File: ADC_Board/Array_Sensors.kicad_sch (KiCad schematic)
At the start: 18 parts, among them U2 PAMC1350DWVR, U3 AMC1400QDWLRQ1, U4 AMC1400QDWLRQ1, U5 PAMC1350DWVR

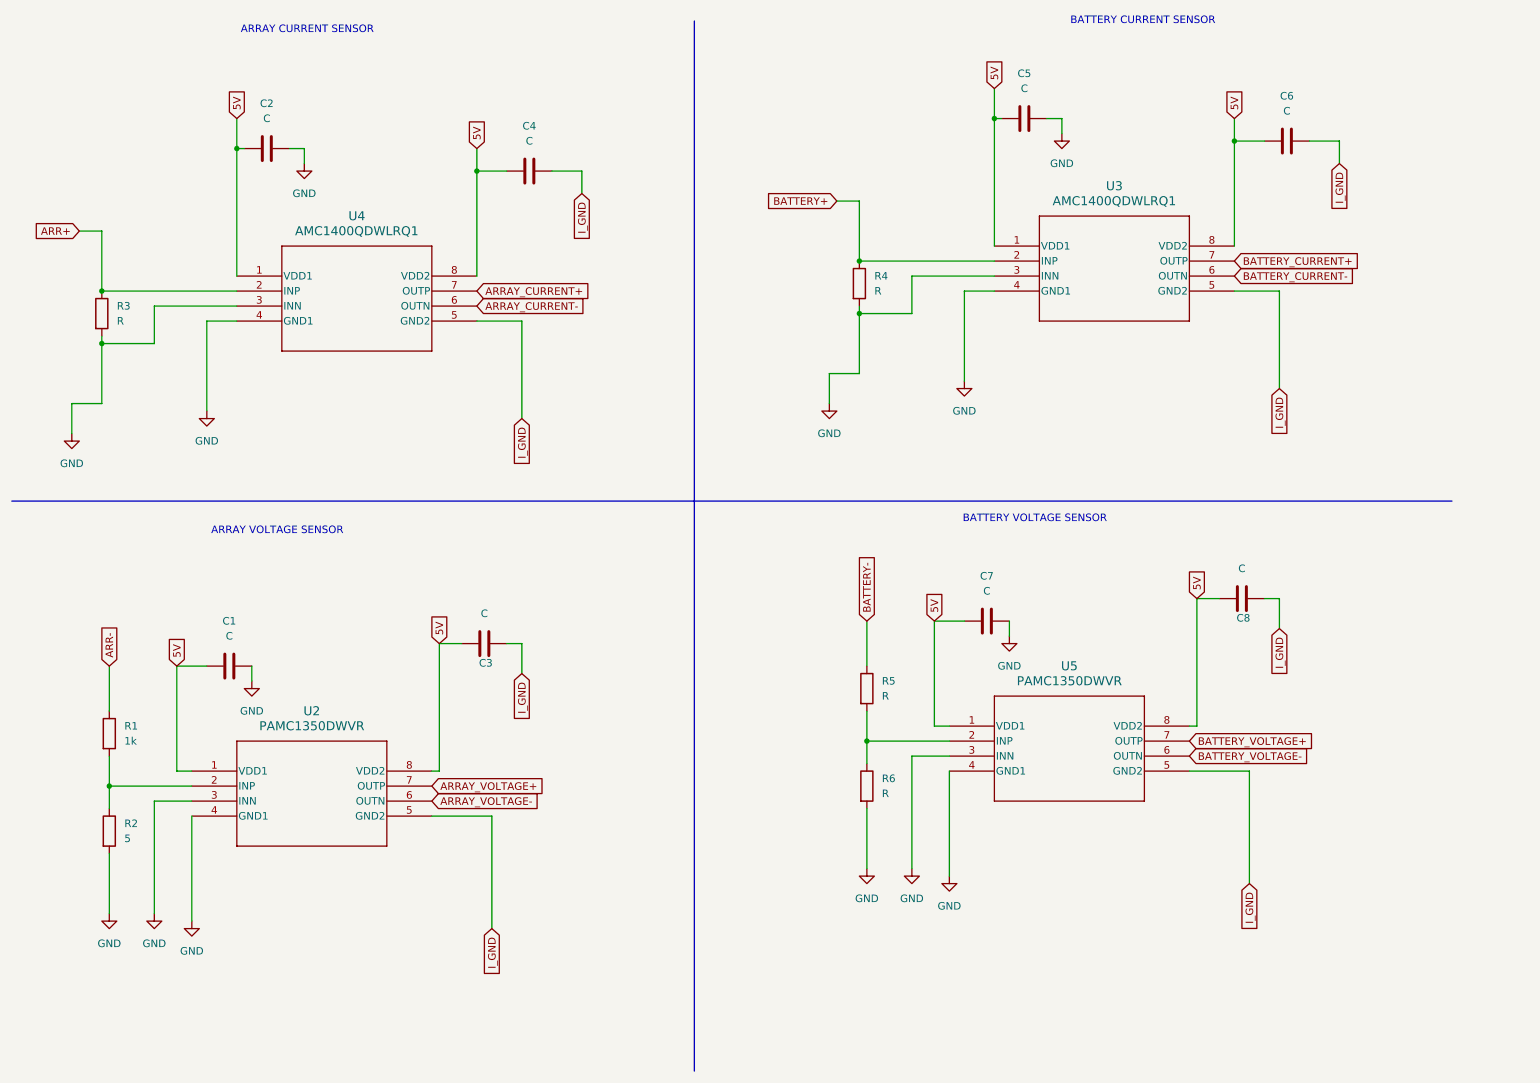
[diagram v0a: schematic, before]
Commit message: Changes made after v1 to address Lakshay and Ishaans comments
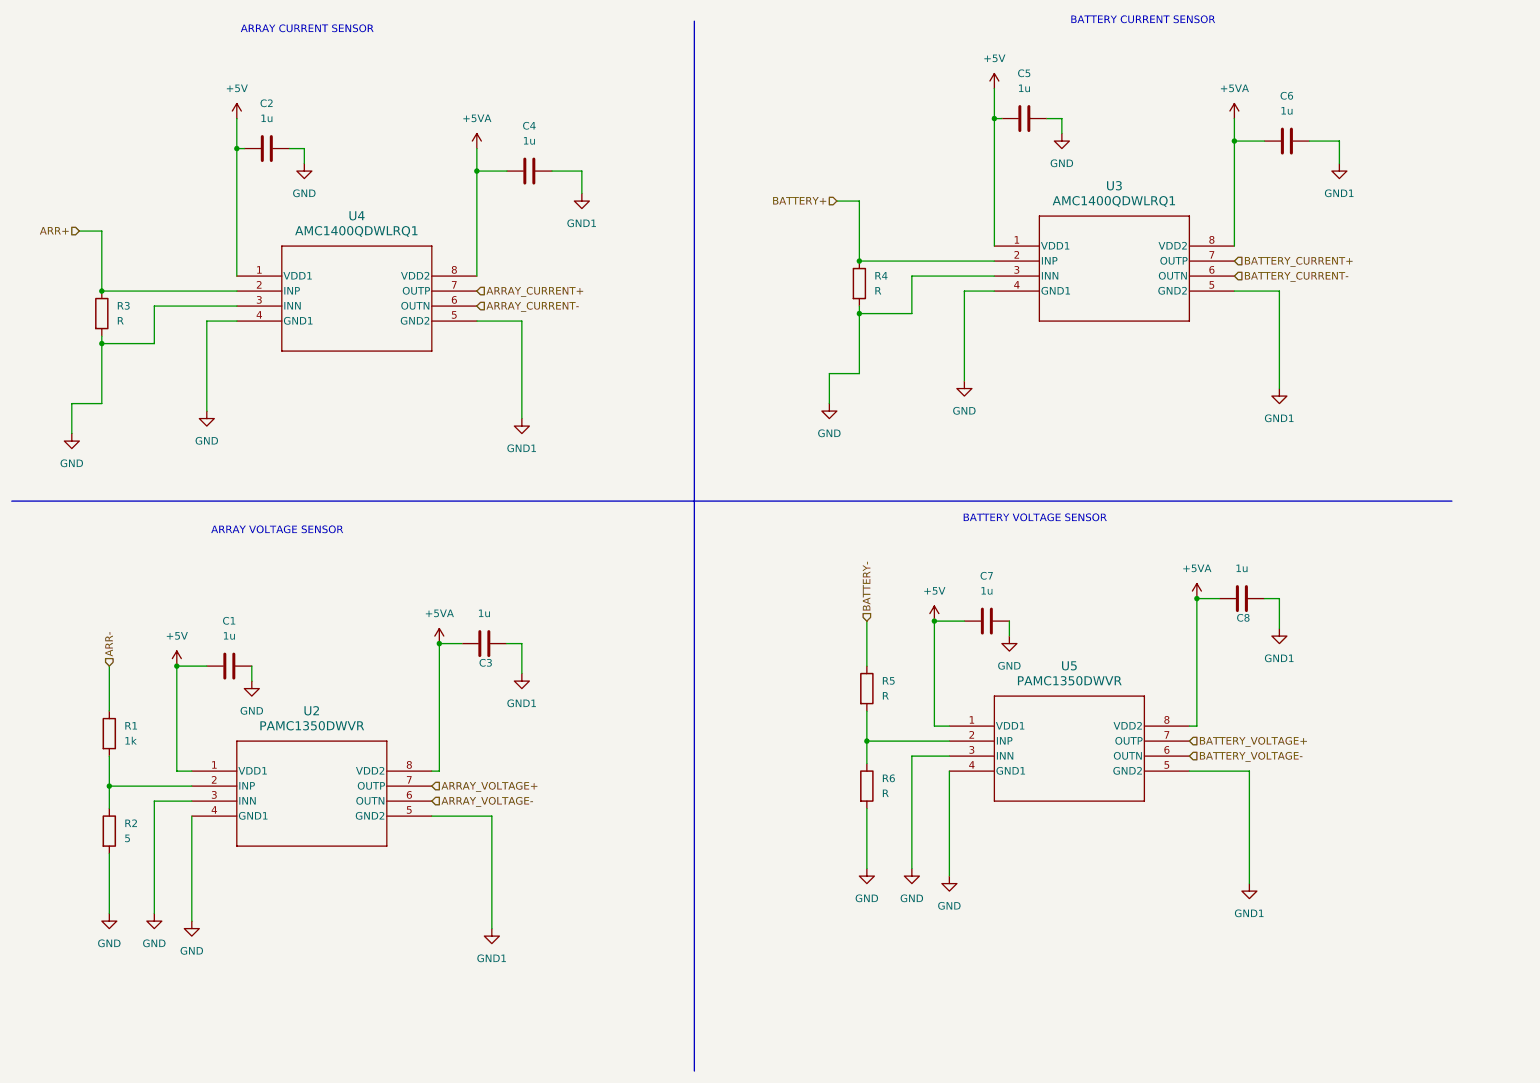
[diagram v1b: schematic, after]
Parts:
- C1, C2, C3, C4, C5, C6, C7, C8: value C -> 1u
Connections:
- net 5V renamed +5V
- net +5V: no longer C3.1, C4.1, C6.1, C8.1, U2.8 (VDD2), U3.8 (VDD2), U4.8 (VDD2), U5.8 (VDD2)
- net I_GND renamed GND1
- new net +5VA: C3.1, C4.1, C6.1, C8.1, U2.8 (VDD2), U3.8 (VDD2), U4.8 (VDD2), U5.8 (VDD2)

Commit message: Added RC filters to first commit of v2 during workday
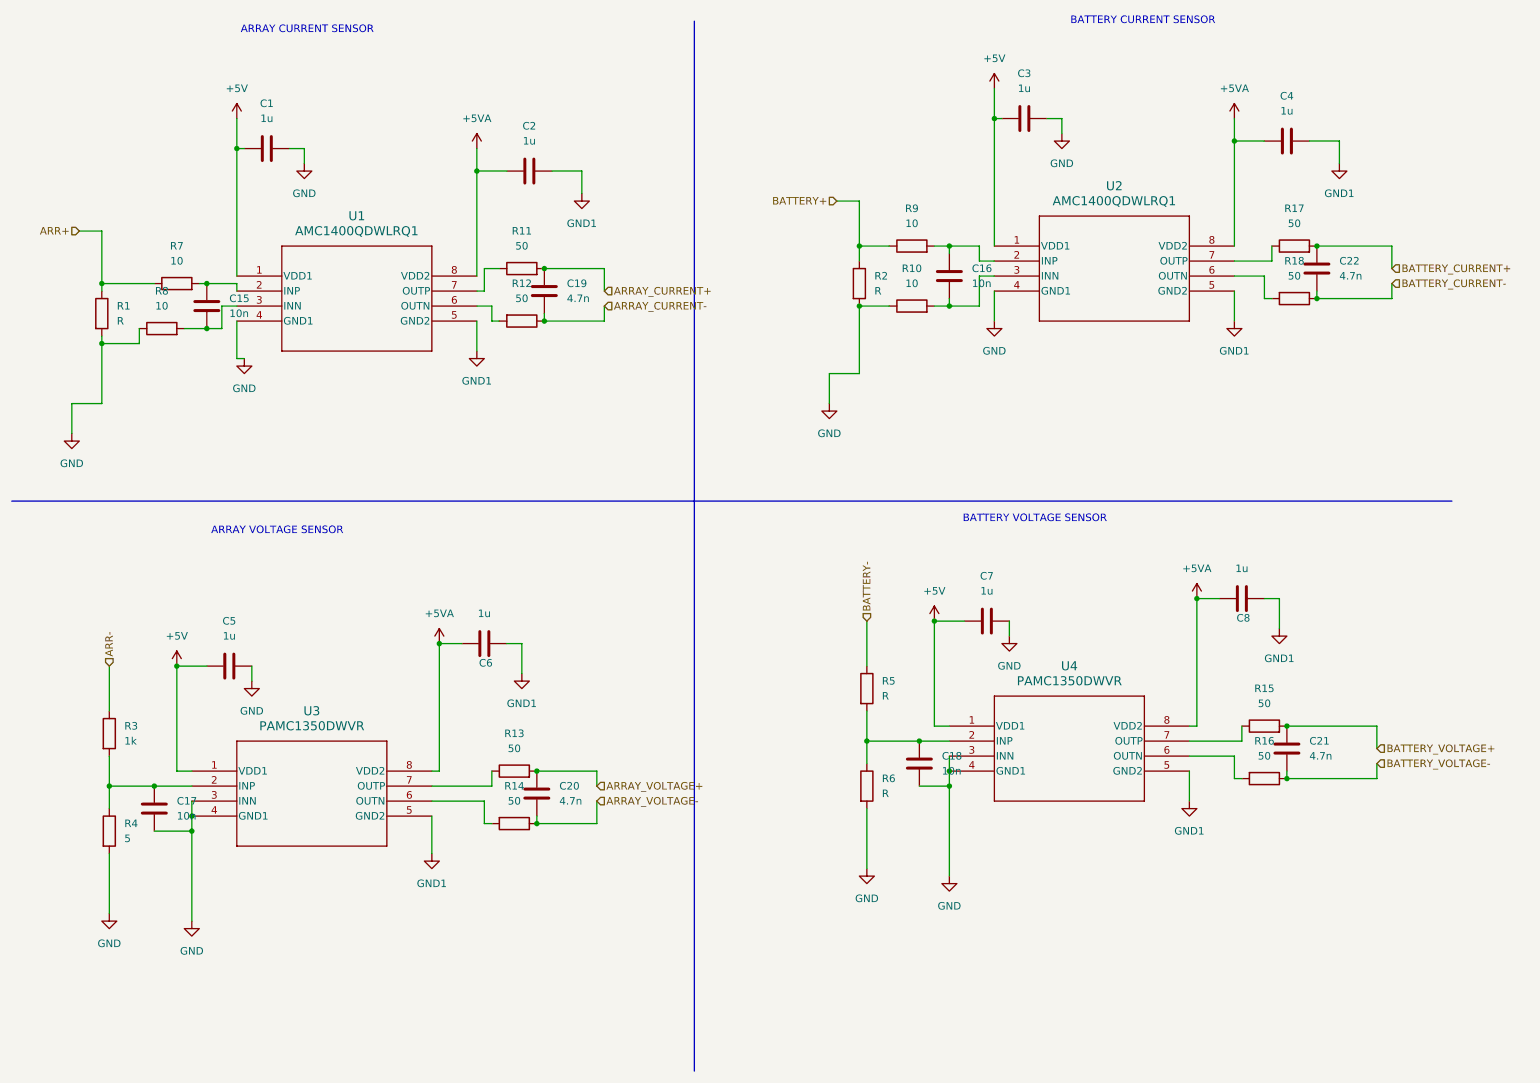
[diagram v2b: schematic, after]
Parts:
- added C15, C16, C17, C18: 10n, symbol Device:C
- added C19, C20, C21, C22: 4.7n, symbol Device:C
- added R10, R7, R8, R9: 10, symbol Device:R
- added R11, R12, R13, R14, R15, R16, R17, R18: 50, symbol Device:R
- renumbered C2 to C1, C4 to C2, C5 to C3, C6 to C4, C1 to C5, C3 to C6, R3 to R1, R4 to R2, R1 to R3, R2 to R4, U4 to U1, U3 to U2, U2 to U3, U5 to U4
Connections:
- net ARR+: now also R7.1; no longer U1.2 (INP)
- net ARRAY_CURRENT+: now also C19.1, R11.2; no longer U1.7 (OUTP)
- net ARRAY_CURRENT-: now also C19.2, R12.1; no longer U1.6 (OUTN)
- net ARRAY_VOLTAGE+: now also C20.1, R13.2; no longer U3.7 (OUTP)
- net ARRAY_VOLTAGE-: now also C20.2, R14.1; no longer U3.6 (OUTN)
- net BATTERY+: now also R9.1; no longer U2.2 (INP)
- net BATTERY_CURRENT+: now also C22.1, R17.2; no longer U2.7 (OUTP)
- net BATTERY_CURRENT-: now also C22.2, R18.1; no longer U2.6 (OUTN)
- net BATTERY_VOLTAGE+: now also C21.1, R15.2; no longer U4.7 (OUTP)
- net BATTERY_VOLTAGE-: now also C21.2, R16.1; no longer U4.6 (OUTN)
- net GND: now also C17.2, C18.2, R10.1, R8.1; no longer U1.3 (INN), U2.3 (INN)
- net at R3.2, R4.1, U3.2 (INP): now also C17.1
- net at R5.2, R6.1, U4.2 (INP): now also C18.1
- new net: R12.2, U1.6 (OUTN)
- new net: C16.2, R10.2, U2.3 (INN)
- new net: R14.2, U3.6 (OUTN)
- new net: R13.1, U3.7 (OUTP)
- new net: C15.1, R7.2, U1.2 (INP)
- new net: C15.2, R8.2, U1.3 (INN)
- new net: R16.2, U4.6 (OUTN)
- new net: R15.1, U4.7 (OUTP)
- new net: R17.1, U2.7 (OUTP)
- new net: R11.1, U1.7 (OUTP)
- new net: C16.1, R9.2, U2.2 (INP)
- new net: R18.2, U2.6 (OUTN)

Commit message: Addressed the comments from Champeys review. Including adding an isolation chip for the SPI. Changing Amplifiers to non-isolating to avoid running signal through ADC twice. As well as a few small changes to pin connections in ADC and DC-DC isolator.
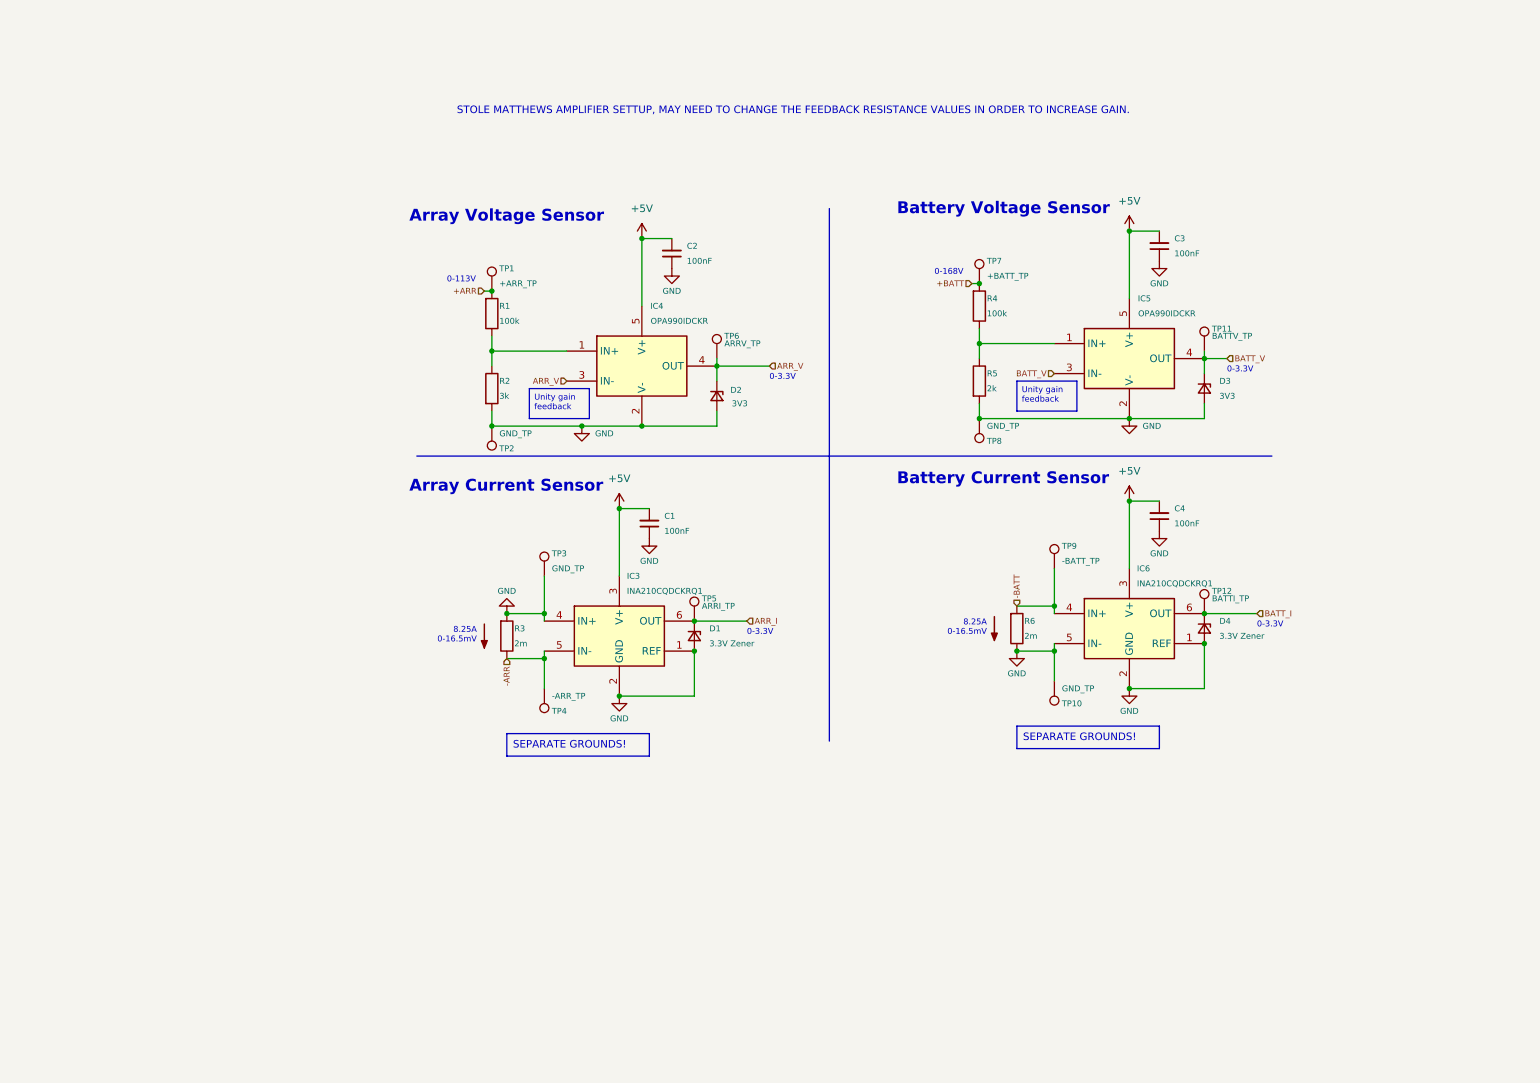
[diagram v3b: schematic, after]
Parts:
- removed C1, C2, C3, C4, C5, C6, C7, C8: 1u, Capacitor_THT:C_Disc_D3.8mm_W2.6mm_P2.50mm, symbol Device:C
- removed C15, C16, C17, C18: 10n, symbol Device:C
- removed C19, C20, C21, C22: 4.7n, symbol Device:C
- removed R10, R7, R8, R9: 10, symbol Device:R
- removed R11, R12, R13, R14, R15, R16, R17, R18: 50, symbol Device:R
- removed U1, U2: AMC1400QDWLRQ1, AMC1400:SOIC_DWLRQ1_TEX, symbol AMC1400 Precision, ±250-mV Input, Reinforced Isolated Amplifier in a 15-mm Stre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
- removed U3, U4: PAMC1350DWVR, U_PAMC1350DWVR_TEX, symbol AMC1350 Precision, ±5-V Input, Reinforced Isolated Amplifier:PAMC1350DWVR
- added C1, C2, C3, C4: 100nF, Capacitor_SMD:C_0402_1005Metric, symbol Device:C_Small
- added D1, D4: 3.3V Zener, Diode_SMD:D_MiniMELF, symbol Device:D_Zener_Small
- added D2, D3: 3V3, Diode_SMD:D_MiniMELF, symbol Device:D_Zener_Small
- added IC3, IC6: INA210CQDCKRQ1, footprints:ti_INA210CQDCKRQ1, symbol ti_INA210CQDCKRQ1:INA210CQDCKRQ1
- added IC4, IC5: OPA990IDCKR, footprints:ti_OPA990IDCKR, symbol ti_OPA990IDCKR:OPA990IDCKR
- added TP1: +ARR_TP, TestPoint:TestPoint_Pad_1.0x1.0mm, symbol Connector:TestPoint
- added TP10, TP2, TP3, TP8: GND_TP, TestPoint:TestPoint_Pad_1.0x1.0mm, symbol Connector:TestPoint
- added TP11: BATTV_TP, TestPoint:TestPoint_Pad_1.0x1.0mm, symbol Connector:TestPoint
- added TP12: BATTI_TP, TestPoint:TestPoint_Pad_1.0x1.0mm, symbol Connector:TestPoint
- added TP4: -ARR_TP, TestPoint:TestPoint_Pad_1.0x1.0mm, symbol Connector:TestPoint
- added TP5: ARRI_TP, TestPoint:TestPoint_Pad_1.0x1.0mm, symbol Connector:TestPoint
- added TP6: ARRV_TP, TestPoint:TestPoint_Pad_1.0x1.0mm, symbol Connector:TestPoint
- added TP7: +BATT_TP, TestPoint:TestPoint_Pad_1.0x1.0mm, symbol Connector:TestPoint
- added TP9: -BATT_TP, TestPoint:TestPoint_Pad_1.0x1.0mm, symbol Connector:TestPoint
- R1: value R -> 100k; footprint (none) -> Resistor_SMD:R_0805_2012Metric; Cost (none) -> 0.0017; Distributor (none) -> JLCPCB; LCSC Part # (none) -> C149504; Manufacturer (none) -> Uniroyal Elec; P/N (none) -> 0805W8F1003T5E
- R2: value R -> 3k; footprint (none) -> Resistor_SMD:R_0805_2012Metric; Cost (none) -> 0.0018; Distributor (none) -> JLCPCB; LCSC Part # (none) -> C17661; Manufacturer (none) -> Uniroyal Elec; P/N (none) -> 0805W8F3001T5E
- R3: value 1k -> 2m; footprint (none) -> Resistor_SMD:R_1206_3216Metric; Cost (none) -> 0.73; Distributor (none) -> Mouser; Manufacturer (none) -> ROHM Semiconductor; P/N (none) -> 755-PMR18EZPFV2L00
- R4: value 5 -> 100k; footprint (none) -> Resistor_SMD:R_0805_2012Metric; Cost (none) -> 0.0017; Distributor (none) -> JLCPCB; LCSC Part # (none) -> C149504; Manufacturer (none) -> Uniroyal Elec; P/N (none) -> 0805W8F1003T5E
- R5: value R -> 2k; footprint (none) -> Resistor_SMD:R_0805_2012Metric; Cost (none) -> 0.0018; Distributor (none) -> JLCPCB; LCSC Part # (none) -> C17604; Manufacturer (none) -> Uniroyal Elec; P/N (none) -> 0805W8F2001T5E
- R6: value R -> 2m; footprint (none) -> Resistor_SMD:R_1206_3216Metric; Cost (none) -> 0.73; Distributor (none) -> Mouser; Manufacturer (none) -> ROHM Semiconductor; P/N (none) -> 755-PMR18EZPFV2L00
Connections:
- net BATTERY+ is gone; now on an unnamed net: R2.1
- net BATTERY- is gone; now on an unnamed net: R5.1
- net +5V: now also C1.2, C2.2, C3.2, C4.2, IC3.3 (V+), IC4.5 (V+), IC5.5 (V+), IC6.3 (V+)
- net GND: now also R3.2, R5.2, R6.1, C1.1, C2.1, C3.1, C4.1, D1.2 (A), D2.2 (A), D3.2 (A), D4.2 (A), IC3.1 (REF), IC3.2 (GND), IC3.4 (IN+), IC4.2 (V-), IC5.2 (V-), IC6.1 (REF), IC6.2 (GND), IC6.5 (IN-), TP10.1, TP2.1, TP3.1, TP8.1; no longer R1.2, R4.2, R6.2
- net at R4.1: now also IC5.1 (IN+); no longer R3.2
- net ARR+: no longer names the net of R1.1
- net ARR+: now also IC4.1 (IN+)
- net ARR- renamed -ARR
- net -ARR: now also IC3.5 (IN-), TP4.1
- new net +ARR: R1.2, TP1.1
- new net +BATT: R4.2, TP7.1
- new net -BATT: IC6.4 (IN+), R6.2, TP9.1
- new net ARR_I: D1.1 (K), IC3.6 (OUT), TP5.1
- new net ARR_V: D2.1 (K), IC4.3 (IN-), IC4.4 (OUT), TP6.1
- new net BATT_I: D4.1 (K), IC6.6 (OUT), TP12.1
- new net BATT_V: D3.1 (K), IC5.3 (IN-), IC5.4 (OUT), TP11.1
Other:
- note added: "0-113V"
- note added: "0-168V"
- note added: "0-3.3V"
- note added: "8.25A 0-16.5mV"
- note added: "Array Current Sensor"
- note added: "Array Voltage Sensor"
- note added: "Battery Current Sensor"
- note added: "Battery Voltage Sensor"
- note added: "STOLE MATTHEWS AMPLIFIER SETTUP, MAY NEED TO CHANGE THE FEEDBACK RESISTANCE VALUES IN ORDER TO INCREASE GAIN."
- note removed: "ARRAY CURRENT SENSOR"
- note removed: "ARRAY VOLTAGE SENSOR"
- note removed: "BATTERY CURRENT SENSOR"
- note removed: "BATTERY VOLTAGE SENSOR"
